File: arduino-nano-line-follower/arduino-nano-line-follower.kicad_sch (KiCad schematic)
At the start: 9 parts, among them J1 l298_input_pins, J2 arduino_vcc_gnd, J3 5v_ir_sensors_pins, J4 gnd_ir_sensors_pins, J5 9v_gnd_l293d, J6 ir_signal, SW2 pwr_switch

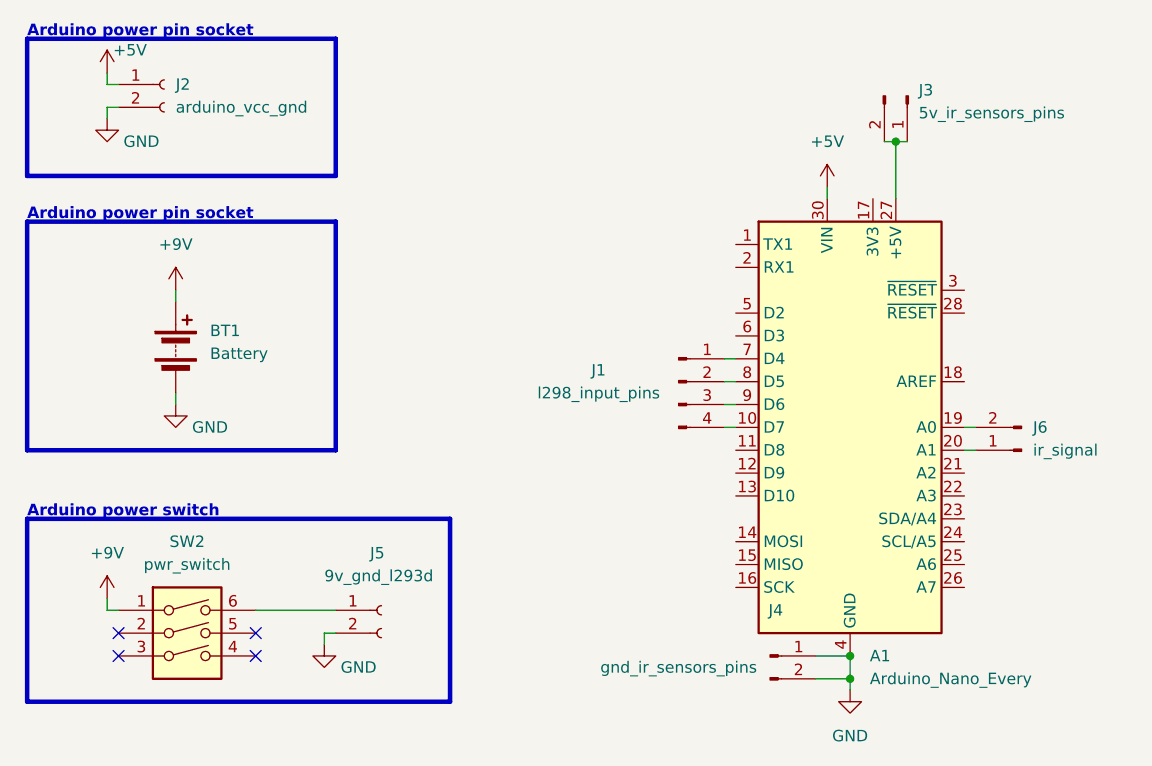
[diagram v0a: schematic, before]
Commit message: project 9 / arduino nano line follower / added pcb
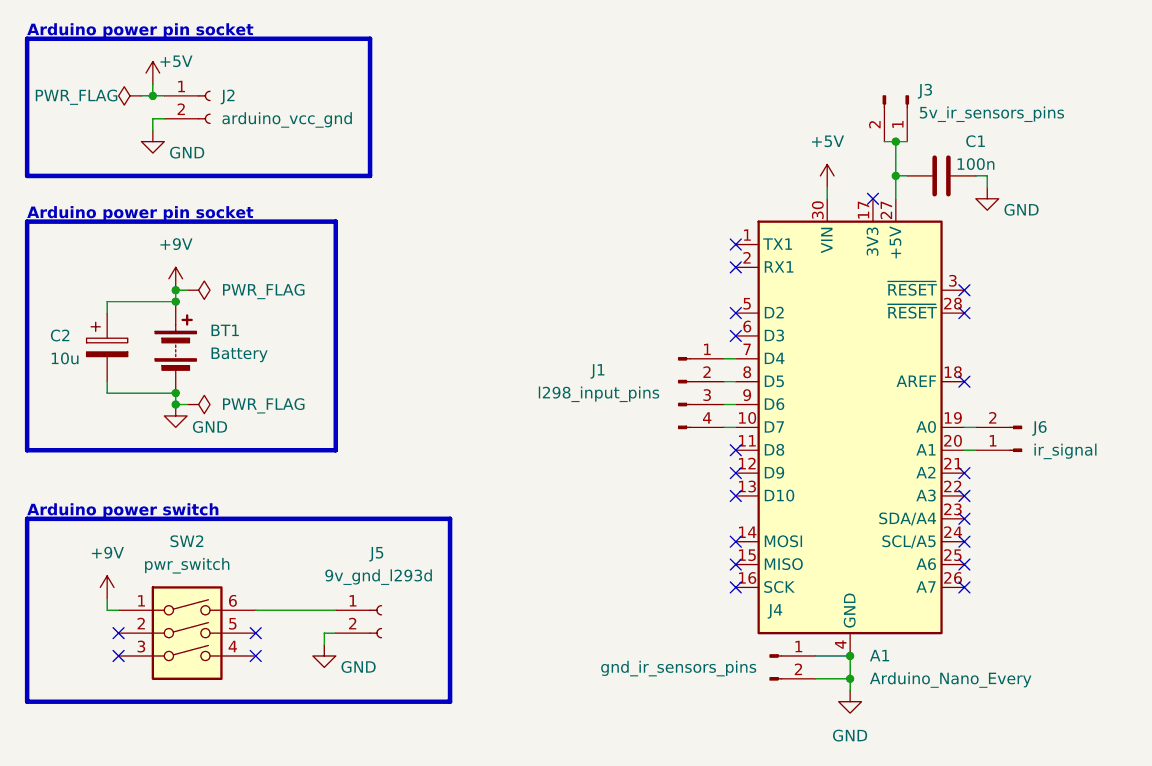
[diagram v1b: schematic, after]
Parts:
- added C1: 100n, Capacitor_THT:C_Disc_D3.0mm_W1.6mm_P2.50mm, symbol Device:C
- added C2: 10u, Capacitor_THT:C_Radial_D4.0mm_H5.0mm_P1.50mm, symbol Device:C_Polarized
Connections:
- net +9V: now also C2.1
- net GND: now also C1.2, C2.2
- net at A1.27 (+5V), J3.1 (Pin_1), J3.2 (Pin_2): now also C1.1
- no-connect marks 4 -> 24
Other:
- moved on the sheet: J2

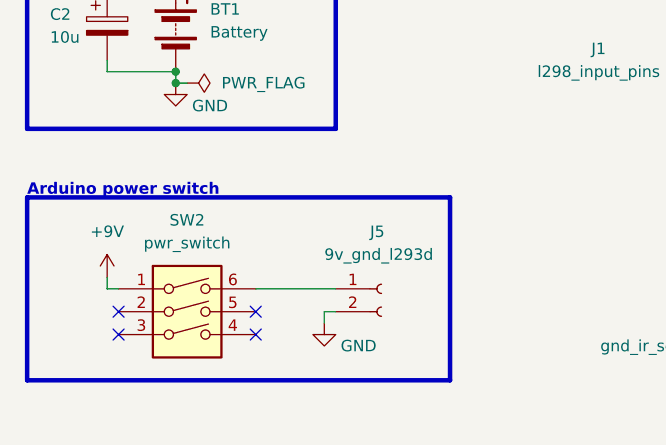
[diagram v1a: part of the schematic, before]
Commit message: project 9 / arduino nano line follower / improved connections
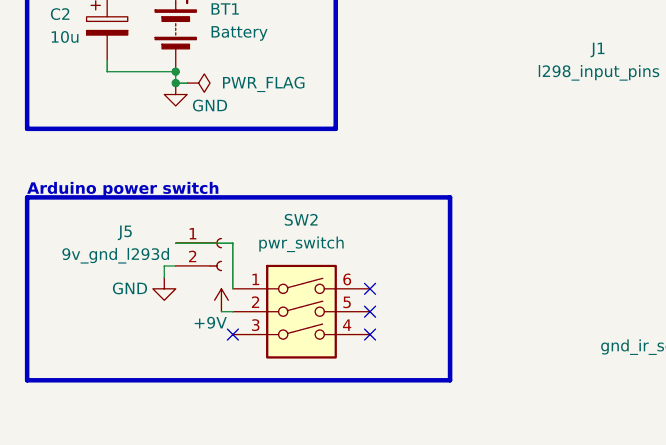
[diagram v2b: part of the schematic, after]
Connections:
- net +9V: now also SW2.2; no longer SW2.1
- net at J5.1 (Pin_1): now also SW2.1; no longer SW2.6
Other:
- moved on the sheet: SW2
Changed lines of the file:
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@@
   (no_connect (at 95.25 49.53))
   (no_connect (at 120.65 72.39))
+  (no_connect (at 54.61 82.55))
   (no_connect (at 95.25 80.01))
   (no_connect (at 95.25 64.77))
   (no_connect (at 110.49 36.83))
   (no_connect (at 95.25 74.93))
-  (no_connect (at 41.91 85.09))
+  (no_connect (at 54.61 85.09))
   (no_connect (at 120.65 69.85))
   (no_connect (at 95.25 44.45))
   (no_connect (at 95.25 52.07))
-  (no_connect (at 26.67 87.63))
+  (no_connect (at 39.37 87.63))
   (no_connect (at 120.65 57.15))
   (no_connect (at 120.65 77.47))
   (no_connect (at 95.25 67.31))
   (no_connect (at 120.65 46.99))
-  (no_connect (at 26.67 85.09))
   (no_connect (at 95.25 77.47))
-  (no_connect (at 41.91 87.63))
+  (no_connect (at 54.61 87.63))
   (no_connect (at 120.65 80.01))
   (no_connect (at 95.25 41.91))
@@
     (stroke (width 0) (type default))
   )
+  (wire (pts (xy 38.1 85.09) (xy 39.37 85.09))
+    (stroke (width 0) (type default))
+  )
   (wire (pts (xy 25.4 49.53) (xy 25.4 48.26))
     (stroke (width 0) (type default))
@@
     (stroke (width 0) (type default))
   )
+  (wire (pts (xy 31.75 80.01) (xy 33.02 80.01))
+    (stroke (width 0) (type default))
+  )
   (wire (pts (xy 33.02 46.99) (xy 33.02 48.26))
     (stroke (width 0) (type default))
@@
     (stroke (width 0) (type default))
   )
+  (wire (pts (xy 39.37 77.47) (xy 39.37 82.55))
+    (stroke (width 0) (type default))
+  )
   (wire (pts (xy 113.03 34.29) (xy 114.3 34.29))
     (stroke (width 0) (type default))
@@
     (stroke (width 0) (type default))
   )
-  (wire (pts (xy 25.4 82.55) (xy 26.67 82.55))
-    (stroke (width 0) (type default))
-  )
   (wire (pts (xy 120.65 62.23) (xy 121.92 62.23))
     (stroke (width 0) (type default))
@@
     (stroke (width 0) (type default))
   )
-  (wire (pts (xy 25.4 82.55) (xy 25.4 81.28))
-    (stroke (width 0) (type default))
-  )
   (wire (pts (xy 25.4 48.26) (xy 33.02 48.26))
     (stroke (width 0) (type default))
@@
     (stroke (width 0) (type default))
   )
-  (wire (pts (xy 50.8 85.09) (xy 49.53 85.09))
-    (stroke (width 0) (type default))
-  )
   (wire (pts (xy 105.41 35.56) (xy 105.41 36.83))
     (stroke (width 0) (type default))
@@
     (stroke (width 0) (type default))
   )
+  (wire (pts (xy 33.02 77.47) (xy 39.37 77.47))
+    (stroke (width 0) (type default))
+  )
+  (wire (pts (xy 31.75 81.28) (xy 31.75 80.01))
+    (stroke (width 0) (type default))
+  )
   (wire (pts (xy 30.48 25.4) (xy 31.75 25.4))
     (stroke (width 0) (type default))
@@
   )
   (wire (pts (xy 30.48 25.4) (xy 30.48 24.13))
-    (stroke (width 0) (type default))
-  )
-  (wire (pts (xy 49.53 85.09) (xy 49.53 86.36))
-    (stroke (width 0) (type default))
-  )
-  (wire (pts (xy 41.91 82.55) (xy 50.8 82.55))
     (stroke (width 0) (type default))
   )
@@
     )
   )
-  (symbol (lib_id "Connector:Conn_01x02_Socket") (at 55.88 82.55 0) (unit 1)
-    (in_bom yes) (on_board yes) (dnp no)
-    (property "Reference" "J5" (at 54.61 76.2 0)
-      (effects (font (size 1.27 1.27)) (justify left))
-    )
-    (property "Value" "9v_gnd_l293d" (at 49.53 78.74 0)
-      (effects (font (size 1.27 1.27)) (justify left))
-    )
-    (property "Footprint" "Connector_PinSocket_2.54mm:PinSocket_1x02_P2.54mm_Vertical" (at 55.88 82.55 0)
-      (effects (font (size 1.27 1.27)) hide)
-    )
-    (property "Datasheet" "~" (at 55.88 82.55 0)
+  (symbol (lib_id "power:GND") (at 31.75 81.28 0) (unit 1)
+    (in_bom yes) (on_board yes) (dnp no)
+    (property "Reference" "#PWR07" (at 31.75 87.63 0)
+      (effects (font (size 1.27 1.27)) hide)
+    )
+    (property "Value" "GND" (at 27.94 82.55 0)
+      (effects (font (size 1.27 1.27)))
+    )
+    (property "Footprint" "" (at 31.75 81.28 0)
+      (effects (font (size 1.27 1.27)) hide)
+    )
+    (property "Datasheet" "" (at 31.75 81.28 0)
+      (effects (font (size 1.27 1.27)) hide)
+    )
+    (pin "1")
+    (instances
+      (project "arduino-nano-line-follower"
+        (path "/fa0a92f7-4760-4ca9-9e66-043071d29047"
+          (reference "#PWR07") (unit 1)
+        )
+      )
+    )
+  )
+  (symbol (lib_id "Connector:Conn_01x02_Pin") (at 114.3 25.4 270) (unit 1)
+    (in_bom yes) (on_board yes) (dnp no) (fields_autoplaced)
+    (property "Reference" "J3" (at 115.57 24.765 90)
+      (effects (font (size 1.27 1.27)) (justify left))
+    )
+    (property "Value" "5v_ir_sensors_pins" (at 115.57 27.305 90)
+      (effects (font (size 1.27 1.27)) (justify left))
+    )
+    (property "Footprint" "Connector_PinHeader_2.54mm:PinHeader_1x02_P2.54mm_Vertical" (at 114.3 25.4 0)
+      (effects (font (size 1.27 1.27)) hide)
+    )
+    (property "Datasheet" "~" (at 114.3 25.4 0)
+      (effects (font (size 1.27 1.27)) hide)
+    )
+    (pin "1")
+    (pin "2")
+    (instances
+      (project "arduino-nano-line-follower"
+        (path "/fa0a92f7-4760-4ca9-9e66-043071d29047"
+          (reference "J3") (unit 1)
+        )
+      )
+    )
+  )
+  (symbol (lib_id "Connector:Conn_01x02_Socket") (at 38.1 77.47 0) (unit 1)
+    (in_bom yes) (on_board yes) (dnp no)
+    (property "Reference" "J5" (at 26.67 76.2 0)
+      (effects (font (size 1.27 1.27)) (justify left))
+    )
+    (property "Value" "9v_gnd_l293d" (at 20.32 78.74 0)
+      (effects (font (size 1.27 1.27)) (justify left))
+    )
+    (property "Footprint" "Connector_PinSocket_2.54mm:PinSocket_1x02_P2.54mm_Vertical" (at 38.1 77.47 0)
+      (effects (font (size 1.27 1.27)) hide)
+    )
+    (property "Datasheet" "~" (at 38.1 77.47 0)
       (effects (font (size 1.27 1.27)) hide)
     )
@@
     )
   )
-  (symbol (lib_id "Connector:Conn_01x02_Pin") (at 114.3 25.4 270) (unit 1)
-    (in_bom yes) (on_board yes) (dnp no) (fields_autoplaced)
-    (property "Reference" "J3" (at 115.57 24.765 90)
-      (effects (font (size 1.27 1.27)) (justify left))
-    )
-    (property "Value" "5v_ir_sensors_pins" (at 115.57 27.305 90)
-      (effects (font (size 1.27 1.27)) (justify left))
-    )
-    (property "Footprint" "Connector_PinHeader_2.54mm:PinHeader_1x02_P2.54mm_Vertical" (at 114.3 25.4 0)
-      (effects (font (size 1.27 1.27)) hide)
-    )
-    (property "Datasheet" "~" (at 114.3 25.4 0)
-      (effects (font (size 1.27 1.27)) hide)
-    )
-    (pin "1")
-    (pin "2")
-    (instances
-      (project "arduino-nano-line-follower"
-        (path "/fa0a92f7-4760-4ca9-9e66-043071d29047"
-          (reference "J3") (unit 1)
-        )
-      )
-    )
-  )
   (symbol (lib_id "power:+9V") (at 33.02 46.99 0) (unit 1)
     (in_bom yes) (on_board yes) (dnp no) (fields_autoplaced)
@@
         (path "/fa0a92f7-4760-4ca9-9e66-043071d29047"
           (reference "J4") (unit 1)
-        )
-      )
-    )
-  )
-  (symbol (lib_id "power:GND") (at 49.53 86.36 0) (unit 1)
-    (in_bom yes) (on_board yes) (dnp no)
-    (property "Reference" "#PWR07" (at 49.53 92.71 0)
-      (effects (font (size 1.27 1.27)) hide)
-    )
-    (property "Value" "GND" (at 53.34 88.9 0)
-      (effects (font (size 1.27 1.27)))
-    )
-    (property "Footprint" "" (at 49.53 86.36 0)
-      (effects (font (size 1.27 1.27)) hide)
-    )
-    (property "Datasheet" "" (at 49.53 86.36 0)
-      (effects (font (size 1.27 1.27)) hide)
-    )
-    (pin "1")
-    (instances
-      (project "arduino-nano-line-follower"
-        (path "/fa0a92f7-4760-4ca9-9e66-043071d29047"
-          (reference "#PWR07") (unit 1)
         )
       )
@@
     )
   )
-  (symbol (lib_id "power:+9V") (at 25.4 81.28 0) (unit 1)
-    (in_bom yes) (on_board yes) (dnp no) (fields_autoplaced)
-    (property "Reference" "#PWR08" (at 25.4 85.09 0)
-      (effects (font (size 1.27 1.27)) hide)
-    )
-    (property "Value" "+9V" (at 25.4 76.2 0)
-      (effects (font (size 1.27 1.27)))
-    )
-    (property "Footprint" "" (at 25.4 81.28 0)
-      (effects (font (size 1.27 1.27)) hide)
-    )
-    (property "Datasheet" "" (at 25.4 81.28 0)
+  (symbol (lib_id "power:+9V") (at 38.1 85.09 0) (unit 1)
+    (in_bom yes) (on_board yes) (dnp no)
+    (property "Reference" "#PWR08" (at 38.1 88.9 0)
+      (effects (font (size 1.27 1.27)) hide)
+    )
+    (property "Value" "+9V" (at 36.83 86.36 0)
+      (effects (font (size 1.27 1.27)))
+    )
+    (property "Footprint" "" (at 38.1 85.09 0)
+      (effects (font (size 1.27 1.27)) hide)
+    )
+    (property "Datasheet" "" (at 38.1 85.09 0)
       (effects (font (size 1.27 1.27)) hide)
     )
@@
     )
   )
-  (symbol (lib_id "Switch:SW_DIP_x03") (at 34.29 87.63 0) (unit 1)
-    (in_bom yes) (on_board yes) (dnp no) (fields_autoplaced)
-    (property "Reference" "SW2" (at 34.29 74.93 0)
-      (effects (font (size 1.27 1.27)))
-    )
-    (property "Value" "pwr_switch" (at 34.29 77.47 0)
-      (effects (font (size 1.27 1.27)))
-    )
-    (property "Footprint" "Button_Switch_THT:SW_NKK_G1xJP" (at 34.29 87.63 0)
-      (effects (font (size 1.27 1.27)) hide)
-    )
-    (property "Datasheet" "~" (at 34.29 87.63 0)
-      (effects (font (size 1.27 1.27)) hide)
-    )
+  (symbol (lib_id "Switch:SW_DIP_x03") (at 46.99 87.63 0) (unit 1)
+    (in_bom yes) (on_board yes) (dnp no) (fields_autoplaced)
+    (property "Reference" "SW2" (at 46.99 74.93 0)
+      (effects (font (size 1.27 1.27)))
+    )
+    (property "Value" "pwr_switch" (at 46.99 77.47 0)
+      (effects (font (size 1.27 1.27)))
+    )
+    (property "Footprint" "Button_Switch_THT:SW_NKK_G1xJP" (at 46.99 87.63 0)
+      (effects (font (size 1.27 1.27)) hide)
+    )
+    (property "Datasheet" "~" (at 46.99 87.63 0)
+      (effects (font (size 1.27 1.27)) hide)
+    )
